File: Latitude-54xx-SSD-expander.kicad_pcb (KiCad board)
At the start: 4 copper layers, 60 x 112 mm, 33 parts, among them J1 Bus_M.2_Socket_M, J2 Bus_M.2_Socket_M, J3 Bus_M.2_Socket_M, J4 qwiic, U1 clockbuffer_9ZXL0651AKLF

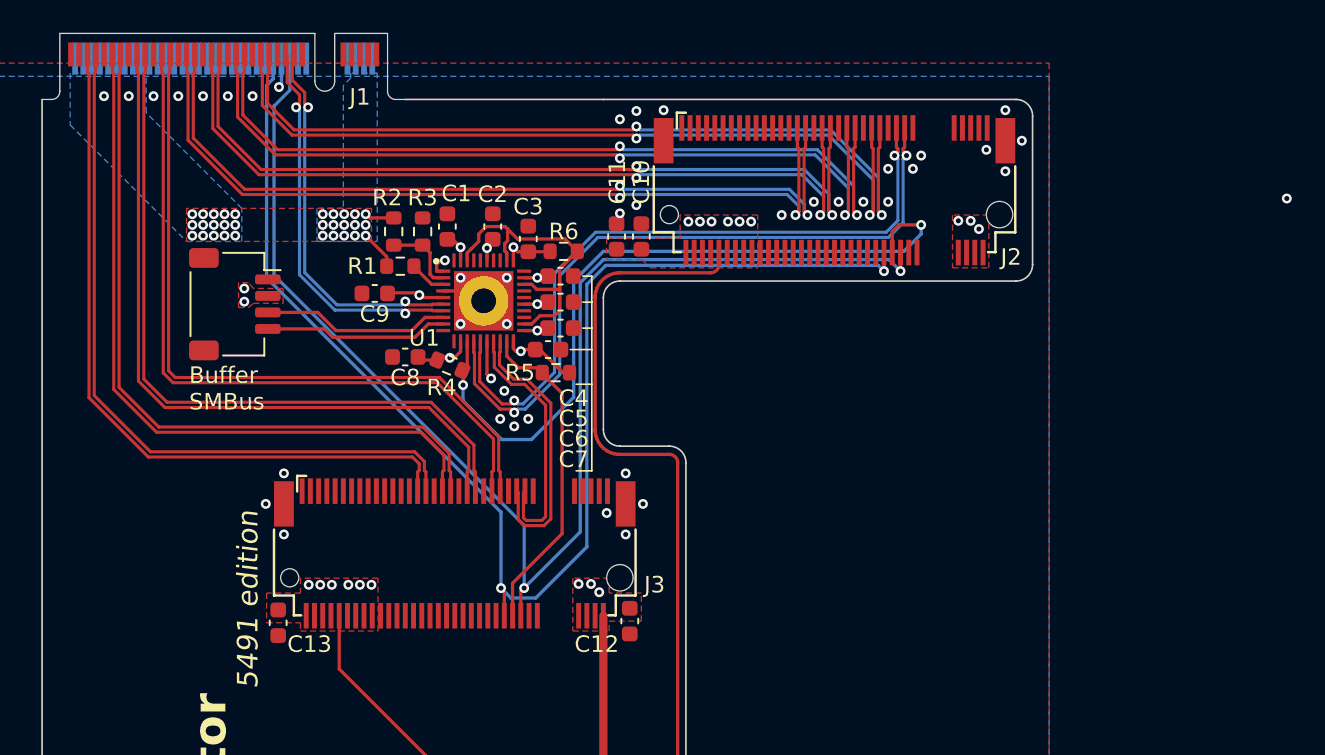
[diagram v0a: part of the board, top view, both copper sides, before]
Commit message: Lots of small fixes to prepare for production
more ground vias,, fixed a diffpair reference layer issue
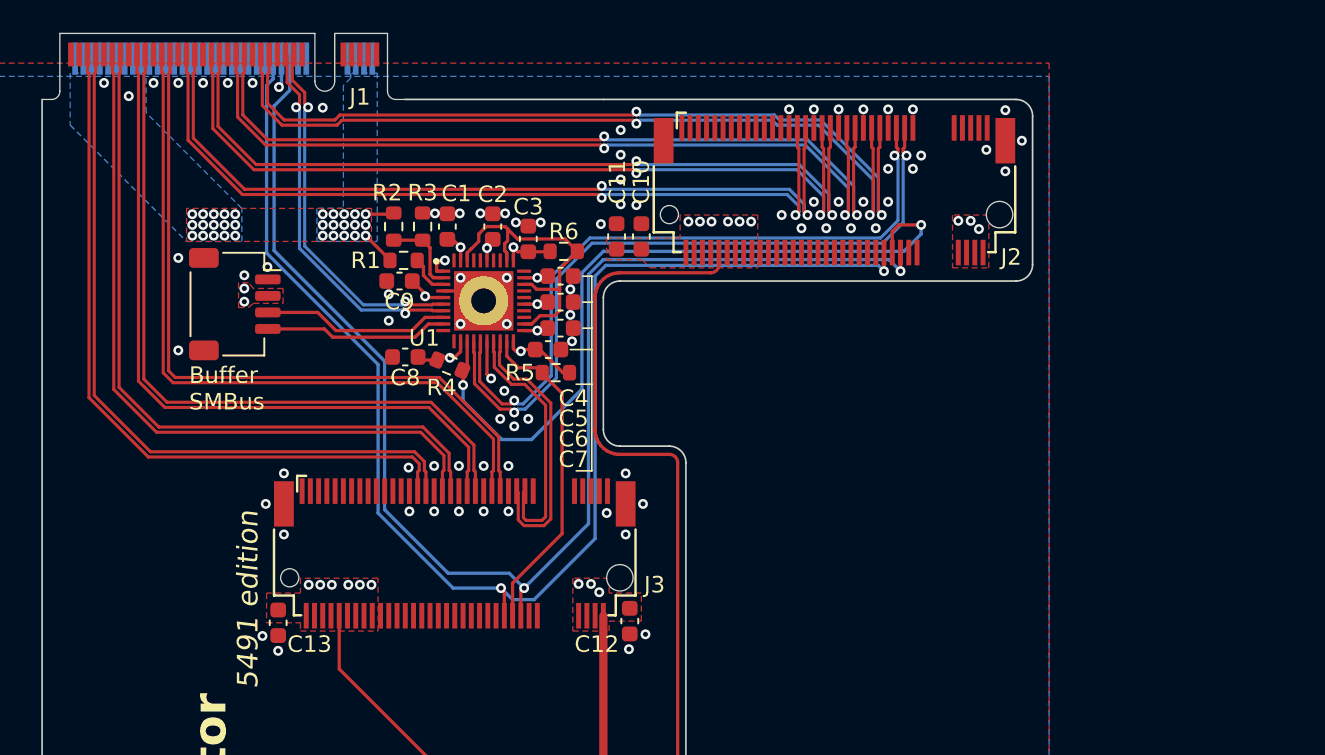
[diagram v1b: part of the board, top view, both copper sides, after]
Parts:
- moved C9 1.68 mm to (100.7, 55.0)
- moved R1 0.40 mm to (100.9, 53.8)
- moved R2 0.30 mm to (100.3, 51.7)
- moved R3 0.30 mm to (102.1, 51.7)
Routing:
- net PEWAKE#: track 81.8 -> 84.0 mm
- net PERST#: track 82.3 -> 84.0 mm
- net +3.3V: track 110.9 -> 109.4 mm
- net Host_REFCLK-: track 23.6 -> 22.7 mm
- net Host_REFCLK+: track 23.1 -> 22.2 mm
- net GND: vias 40 -> 81
- net (no net): vias 1 -> 0
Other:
- board text added: "TODO: [x] Properly look into the mounting method to the chassis -[ ] Cut off unused PCB area near the end [x] Come up with a better name/logo [x] diffpair ground vias [x] M.2 slot capacitors -[ ] remove ground around diffpairs? [x] more ground vias"
- board text removed: "TODO: [ ] Properly look into the mounting method to the chassis [ ] Cut off unused PCB area near the end [ ] Come up with a better name/logo [?] diffpair ground vias [x] M.2 slot capacitors [ ] remove ground around diffpairs? [ ] more ground vias"

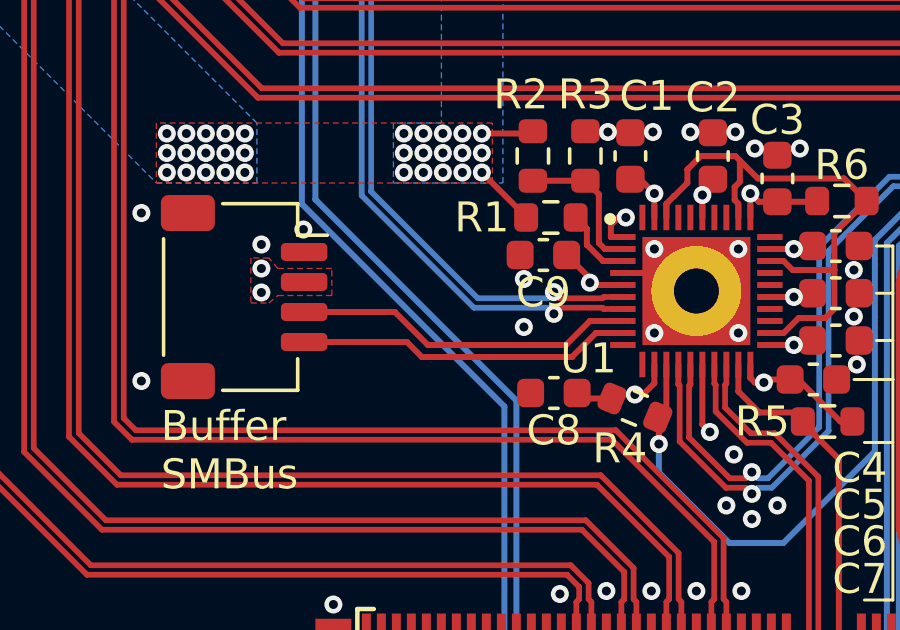
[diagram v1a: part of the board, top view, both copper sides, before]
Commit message: Added i2c pullups
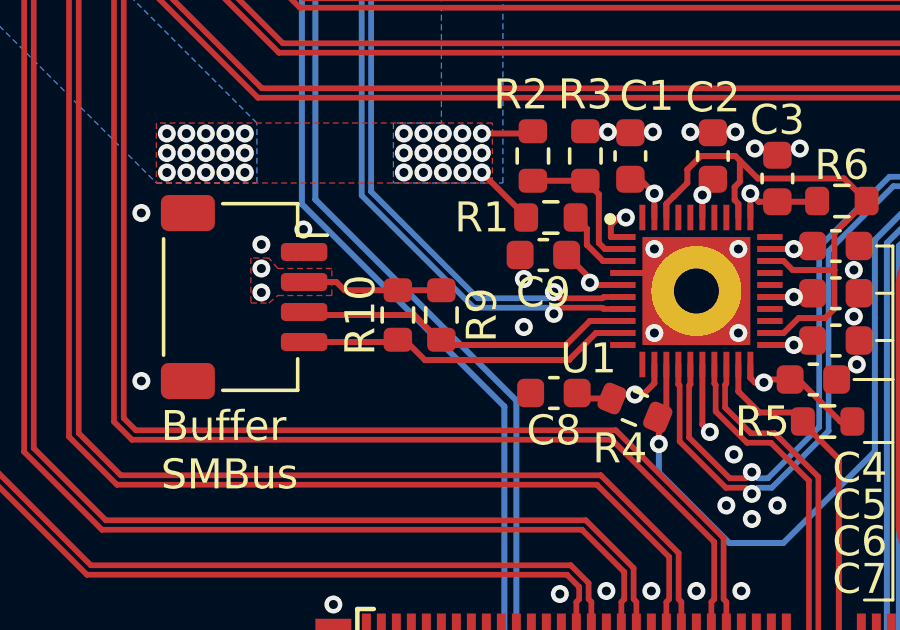
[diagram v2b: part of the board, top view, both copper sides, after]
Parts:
- added R10: 10kΩ, Resistor_SMD:R_0603_1608Metric, F.Cu at (95.8, 57.0)
- added R9: 10kΩ, Resistor_SMD:R_0603_1608Metric, F.Cu at (97.2, 57.0)
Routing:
- net +3.3V: track 109.4 -> 114.1 mm

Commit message: edge vias
for some reason, they probably look cool
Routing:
- net GND: vias 81 -> 202
